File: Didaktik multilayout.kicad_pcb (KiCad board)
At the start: 2 copper layers, 209.6 x 76.2 mm, 125 parts, among them J1 Conn_01x04_MountingPin, J2 AVR-ISP-6, J3 Conn_01x03, SW1 SW_Push_45deg, SW10 SW_Push_45deg, SW11 SW_Push_45deg, SW12 SW_Push_45deg, SW13 SW_Push_45deg, SW14 SW_Push_45deg, SW15 SW_Push_45deg, SW16 SW_Push_45deg, SW17 SW_Push_45deg, SW18 SW_Push_45deg, SW19 SW_Push_45deg, SW2 SW_Push_45deg, SW20 SW_Push_45deg, SW21 SW_Push_45deg, SW22 SW_Push_45deg, SW23 SW_Push_45deg, SW24 SW_Push_45deg, SW25 SW_Push_45deg, SW26 SW_Push_45deg, SW27 SW_Push_45deg, SW28 SW_Push_45deg, SW29 SW_Push_45deg, SW3 SW_Push_45deg, SW30 SW_Push_45deg, SW31 SW_Push_45deg, SW31a1 SW_Push_45deg, SW32 SW_Push_45deg, SW32a1 SW_Push_45deg, SW33 SW_Push_45deg, SW33a1 SW_Push_45deg, SW34 SW_Push_45deg, SW34a1 SW_Push_45deg, SW34b1 SW_Push_45deg, SW35 SW_Push_45deg, SW35a1 SW_Push_45deg, SW35b1 SW_Push_45deg, SW35c1 SW_Push_45deg, SW36 SW_Push_45deg, SW36a1 SW_Push_45deg, SW36b1 SW_Push_45deg, SW36c1 SW_Push_45deg, SW37 SW_Push_45deg, SW37a1 SW_Push_45deg, SW37b1 SW_Push_45deg, SW38 SW_Push_45deg, SW38a1 SW_Push_45deg, SW39 SW_Push_45deg, SW39a1 SW_Push_45deg, SW4 SW_Push_45deg, SW40 SW_Push_45deg, SW40a1 SW_Push_45deg, SW41 RotaryEncoder_Switch, SW42 RotaryEncoder_Switch, SW5 SW_Push_45deg, SW6 SW_Push_45deg, SW7 SW_Push_45deg, SW8 SW_Push_45deg, SW9 SW_Push_45deg, U1 ATmega32U4-M, Y1 Crystal_GND24_Small

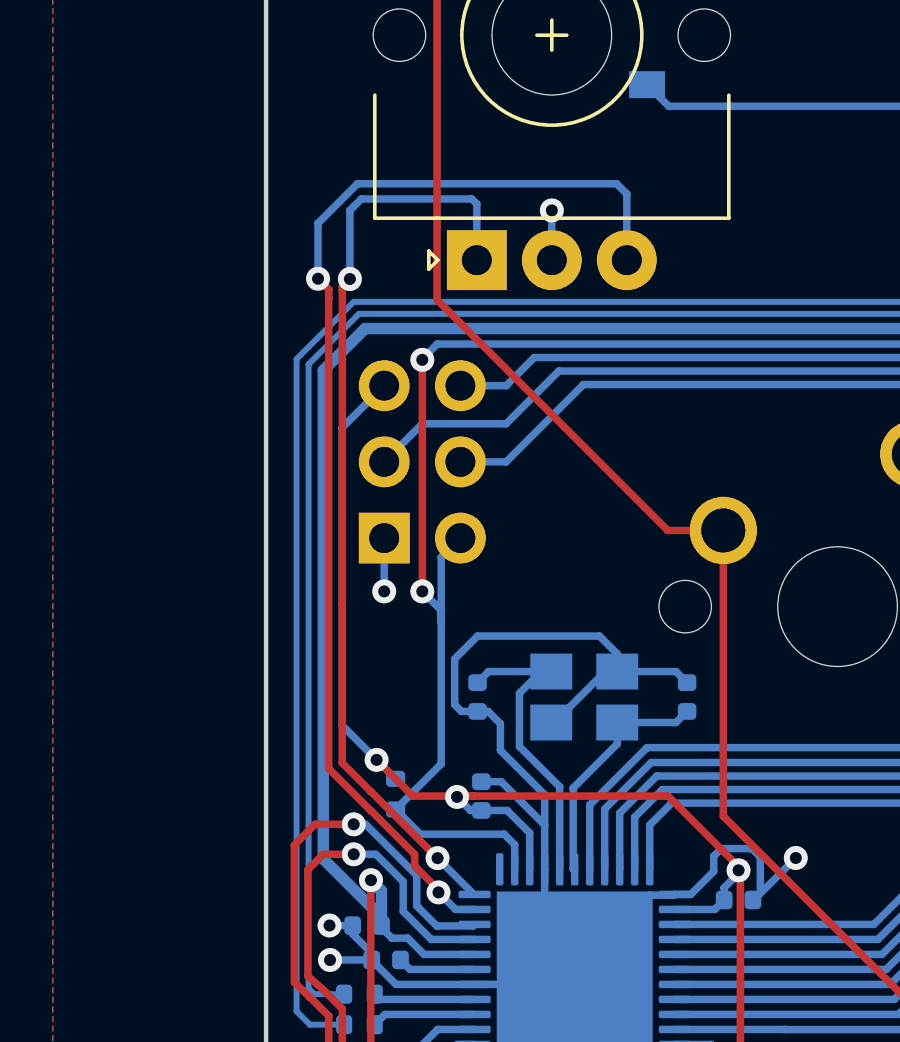
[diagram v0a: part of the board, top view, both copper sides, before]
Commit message: trying to export plate files
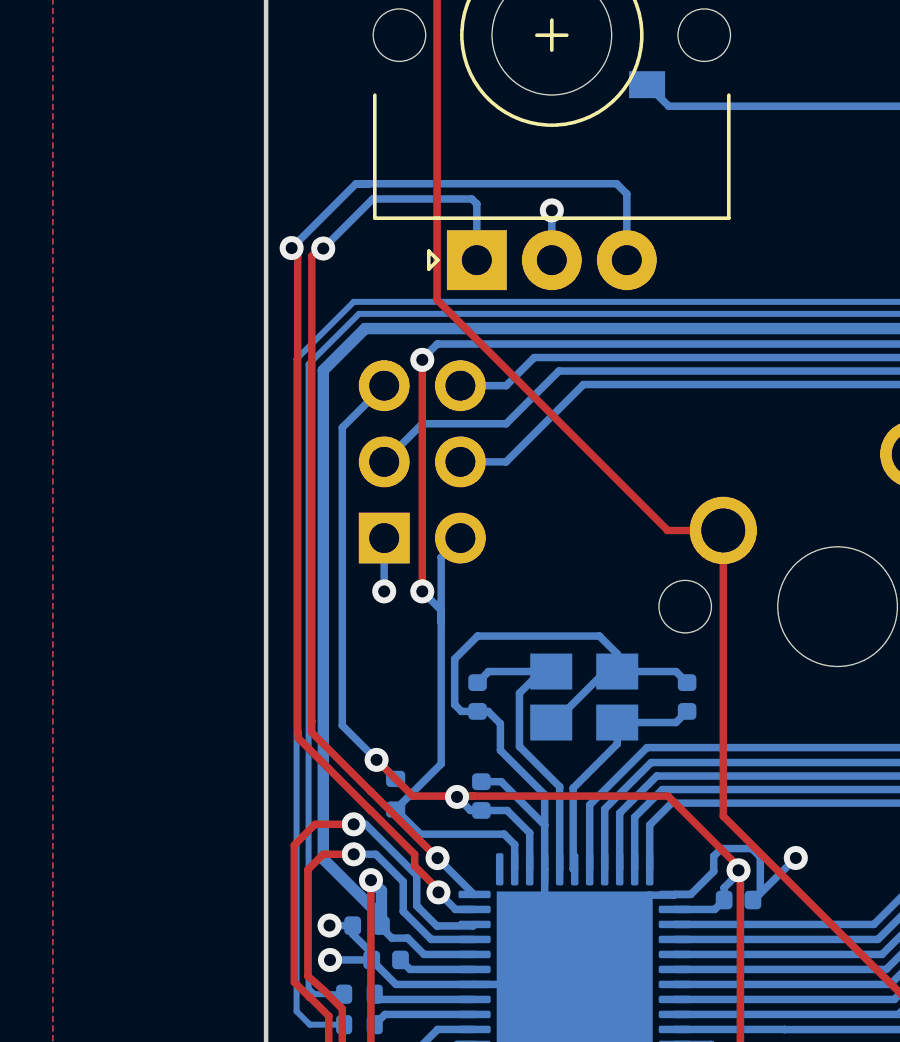
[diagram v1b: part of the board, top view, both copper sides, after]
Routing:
- net ROTARY_B: track 38.6 -> 39.8 mm
- net ROTARY_A: track 31.1 -> 31.8 mm
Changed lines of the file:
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@@
   (segment (start 47.018 70.104) (end 47.018 69.695) (width 0.25) (layer "B.Cu") (net 57))
   (segment (start 35.687 52.959) (end 34.29 54.356) (width 0.25) (layer "B.Cu") (net 57))
-  (segment (start 37.465 68.707) (end 35.245398 66.487398) (width 0.25) (layer "F.Cu") (net 58))
-  (segment (start 34.29 60.198) (end 34.29 49.784) (width 0.25) (layer "F.Cu") (net 58))
-  (segment (start 34.29 49.784) (end 34.29 49.657) (width 0.25) (layer "F.Cu") (net 58))
-  (segment (start 35.245398 66.487398) (end 35.239602 66.487398) (width 0.25) (layer "F.Cu") (net 58))
-  (segment (start 35.239602 66.487398) (end 34.287102 65.534898) (width 0.25) (layer "F.Cu") (net 58))
-  (segment (start 34.287102 60.200898) (end 34.29 60.198) (width 0.25) (layer "F.Cu") (net 58))
-  (segment (start 34.287102 65.534898) (end 34.287102 60.200898) (width 0.25) (layer "F.Cu") (net 58))
-  (segment (start 34.29 49.657) (end 34.544 49.403) (width 0.25) (layer "F.Cu") (net 58))
-  (via (at 34.544 49.403) (size 0.8) (drill 0.4) (layers "F.Cu" "B.Cu") (net 58))
+  (segment (start 33.528 48.387) (end 33.655 48.387) (width 0.25) (layer "F.Cu") (net 58))
+  (segment (start 33.274 64.135) (end 33.274 64.521796) (width 0.25) (layer "F.Cu") (net 58))
+  (segment (start 33.274 48.641) (end 33.528 48.387) (width 0.25) (layer "F.Cu") (net 58))
+  (segment (start 35.239602 66.487398) (end 35.245398 66.487398) (width 0.25) (layer "F.Cu") (net 58))
+  (segment (start 35.245398 66.487398) (end 37.465 68.707) (width 0.25) (layer "F.Cu") (net 58))
+  (segment (start 33.274 64.135) (end 33.274 48.641) (width 0.25) (layer "F.Cu") (net 58))
+  (segment (start 33.274 64.521796) (end 35.239602 66.487398) (width 0.25) (layer "F.Cu") (net 58))
+  (via (at 33.655 48.387) (size 0.8) (drill 0.4) (layers "F.Cu" "B.Cu") (net 58))
   (via (at 37.465 68.707) (size 0.8) (drill 0.4) (layers "F.Cu" "B.Cu") (net 58))
+  (segment (start 38.775 46.903) (end 38.775 48.775) (width 0.25) (layer "B.Cu") (net 58))
   (segment (start 38.67575 69.91775) (end 37.465 68.707) (width 0.25) (layer "B.Cu") (net 58))
-  (segment (start 34.544 49.403) (end 34.544 47.117) (width 0.25) (layer "B.Cu") (net 58))
-  (segment (start 34.544 47.117) (end 34.671 46.99) (width 0.25) (layer "B.Cu") (net 58))
   (segment (start 38.608 46.736) (end 38.775 46.903) (width 0.25) (layer "B.Cu") (net 58))
-  (segment (start 34.925 46.736) (end 38.608 46.736) (width 0.25) (layer "B.Cu") (net 58))
-  (segment (start 38.775 46.903) (end 38.775 48.775) (width 0.25) (layer "B.Cu") (net 58))
-  (segment (start 34.671 46.99) (end 34.925 46.736) (width 0.25) (layer "B.Cu") (net 58))
+  (segment (start 35.306 46.736) (end 38.608 46.736) (width 0.25) (layer "B.Cu") (net 58))
+  (segment (start 33.655 48.387) (end 35.306 46.736) (width 0.25) (layer "B.Cu") (net 58))
   (segment (start 38.6995 69.91775) (end 38.67575 69.91775) (width 0.25) (layer "B.Cu") (net 58))
   (segment (start 151.765 95.885) (end 147.0025 95.885) (width 0.25) (layer "F.Cu") (net 59))
@@
   (segment (start 48.729188 81.45) (end 43.853812 81.45) (width 0.25) (layer "B.Cu") (net 76))
   (segment (start 94.615 76.835) (end 90.054 72.274) (width 0.25) (layer "B.Cu") (net 76))
+  (segment (start 32.824 64.708192) (end 32.824 64.516) (width 0.25) (layer "F.Cu") (net 77))
   (segment (start 35.238904 67.123096) (end 33.837102 65.721294) (width 0.25) (layer "F.Cu") (net 77))
-  (segment (start 33.837102 50.040898) (end 33.84 50.038) (width 0.25) (layer "F.Cu") (net 77))
+  (segment (start 33.837102 65.721294) (end 32.824 64.708192) (width 0.25) (layer "F.Cu") (net 77))
+  (segment (start 32.803 48.661503) (end 32.528497 48.387) (width 0.25) (layer "F.Cu") (net 77))
+  (segment (start 32.803 64.495) (end 32.803 48.661503) (width 0.25) (layer "F.Cu") (net 77))
   (segment (start 36.702302 68.969607) (end 36.702302 68.580698) (width 0.25) (layer "F.Cu") (net 77))
   (segment (start 37.4965 69.763805) (end 36.702302 68.969607) (width 0.25) (layer "F.Cu") (net 77))
-  (segment (start 33.837102 65.721294) (end 33.837102 50.040898) (width 0.25) (layer "F.Cu") (net 77))
-  (segment (start 33.84 49.753136) (end 33.48093 49.394066) (width 0.25) (layer "F.Cu") (net 77))
-  (segment (start 33.84 50.038) (end 33.84 49.753136) (width 0.25) (layer "F.Cu") (net 77))
+  (segment (start 32.824 64.516) (end 32.803 64.495) (width 0.25) (layer "F.Cu") (net 77))
+  (segment (start 32.586245 48.387) (end 32.601318 48.371927) (width 0.25) (layer "F.Cu") (net 77))
+  (segment (start 32.528497 48.387) (end 32.586245 48.387) (width 0.25) (layer "F.Cu") (net 77))
   (segment (start 37.4965 69.85) (end 37.4965 69.763805) (width 0.25) (layer "F.Cu") (net 77))
   (segment (start 36.702302 68.580698) (end 35.248799 67.127195) (width 0.25) (layer "F.Cu") (net 77))
   (via (at 37.4965 69.85) (size 0.8) (drill 0.4) (layers "F.Cu" "B.Cu") (net 77))
-  (via (at 33.48093 49.394066) (size 0.8) (drill 0.4) (layers "F.Cu" "B.Cu") (net 77))
+  (via (at 32.601318 48.371927) (size 0.8) (drill 0.4) (layers "F.Cu" "B.Cu") (net 77))
   (arc (start 35.248799 67.127195) (mid 35.244259 67.124161) (end 35.238904 67.123096) (width 0.25) (layer "F.Cu") (net 77))
   (segment (start 43.775 46.569) (end 43.775 48.775) (width 0.25) (layer "B.Cu") (net 77))
-  (segment (start 33.48093 47.543674) (end 34.796604 46.228) (width 0.25) (layer "B.Cu") (net 77))
-  (segment (start 34.796604 46.228) (end 43.434 46.228) (width 0.25) (layer "B.Cu") (net 77))
   (segment (start 38.6995 70.41775) (end 38.06425 70.41775) (width 0.25) (layer "B.Cu") (net 77))
+  (segment (start 32.601318 48.371927) (end 34.745245 46.228) (width 0.25) (layer "B.Cu") (net 77))
+  (segment (start 34.796604 46.228) (end 34.925 46.228) (width 0.25) (layer "B.Cu") (net 77))
   (segment (start 38.06425 70.41775) (end 37.4965 69.85) (width 0.25) (layer "B.Cu") (net 77))
-  (segment (start 33.48093 49.394066) (end 33.48093 47.543674) (width 0.25) (layer "B.Cu") (net 77))
+  (segment (start 34.745245 46.228) (end 35.179 46.228) (width 0.25) (layer "B.Cu") (net 77))
   (segment (start 43.434 46.228) (end 43.775 46.569) (width 0.25) (layer "B.Cu") (net 77))
+  (segment (start 34.925 46.228) (end 35.179 46.228) (width 0.25) (layer "B.Cu") (net 77))
+  (segment (start 35.179 46.228) (end 43.434 46.228) (width 0.25) (layer "B.Cu") (net 77))
   (segment (start 34.29 78.613) (end 34.654503 78.977503) (width 0.25) (layer "F.Cu") (net 78))
   (segment (start 33.655 68.58) (end 33.1405 69.0945) (width 0.25) (layer "F.Cu") (net 78))

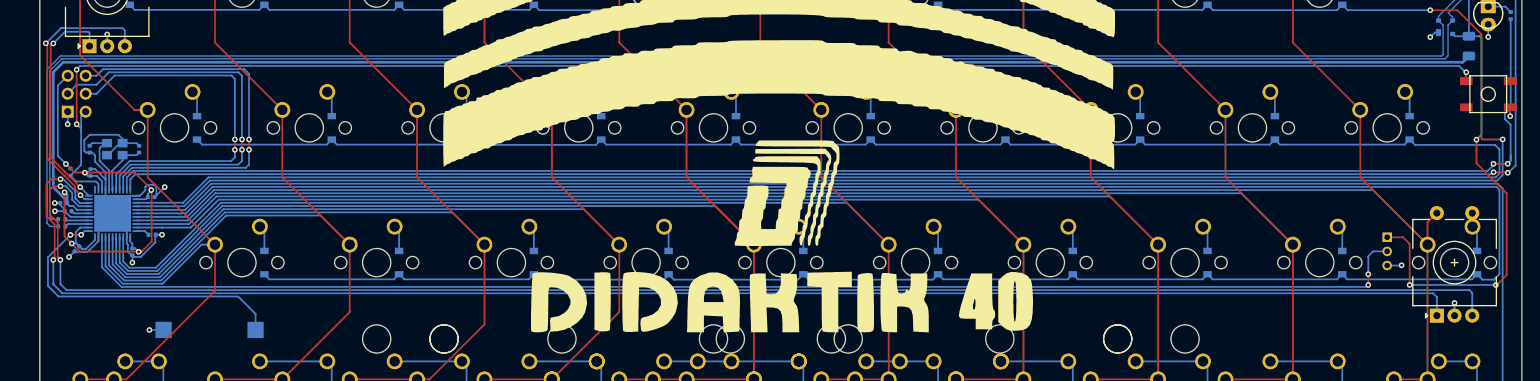
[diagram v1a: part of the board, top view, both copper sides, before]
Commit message: edited buzzer schematics & pcb placement
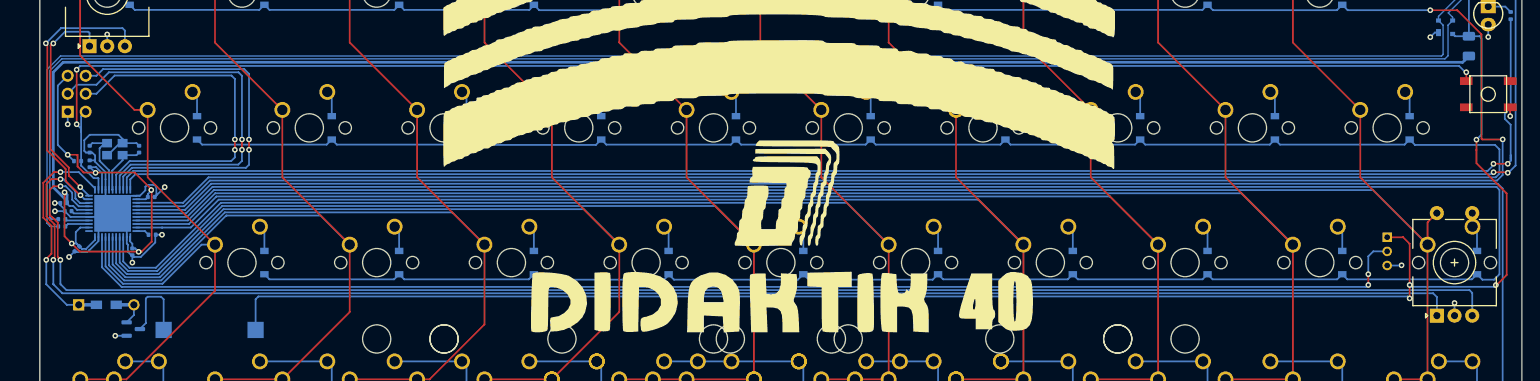
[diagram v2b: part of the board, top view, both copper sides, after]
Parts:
- added Q1: 2N2222, Package_TO_SOT_SMD:SOT-23, B.Cu at (45.0, 88.8)
- added R5: 1k, Keebio-Parts:Diode-Hybrid-Back, F.Cu at (41.1, 85.3)
- moved R3 1.85 mm to (37.1, 65.0), turned to 0 degrees
- moved C1 1.24 mm to (38.8, 65.4)
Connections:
- LS1 pad 1: Net-(U1-Pad1) -> VCC
- LS1 pad 2: GND -> Net-(LS1-Pad2)
- U1 pad 1: Net-(U1-Pad1) -> unconnected-(U1-Pad1)
- U1 pad 12: unconnected-(U1-Pad12) -> Net-(R5-Pad1)
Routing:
- net VCC: track 84.0 -> 253.6 mm, vias 3 -> 4
- net Net-(U1-Pad1): track 44.6 -> 0.00 mm, vias 2 -> 0
- net Net-(R5-Pad1): track 0.00 -> 30.0 mm, vias 0 -> 2
- net Net-(LS1-Pad2): track 0.00 -> 11.8 mm
- net Net-(Q1-Pad2): track 0.00 -> 2.90 mm
- net RESET: track 222.6 -> 220.0 mm
- net GND: track 91.4 -> 89.1 mm
- net +5V: track 301.0 -> 302.3 mm

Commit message: new production files
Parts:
- added R6: 1k, Resistor_SMD:R_0402_1005Metric, B.Cu at (55.8, 84.5)
- moved LS1 0.89 mm to (55.8, 89.8)
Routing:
- net VCC: track 253.6 -> 261.2 mm
- net Net-(Q1-Pad3): track 11.8 -> 19.1 mm
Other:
- board text added: "RESET"
- board text added: "resistor buzzer"
- board text removed: "JST"

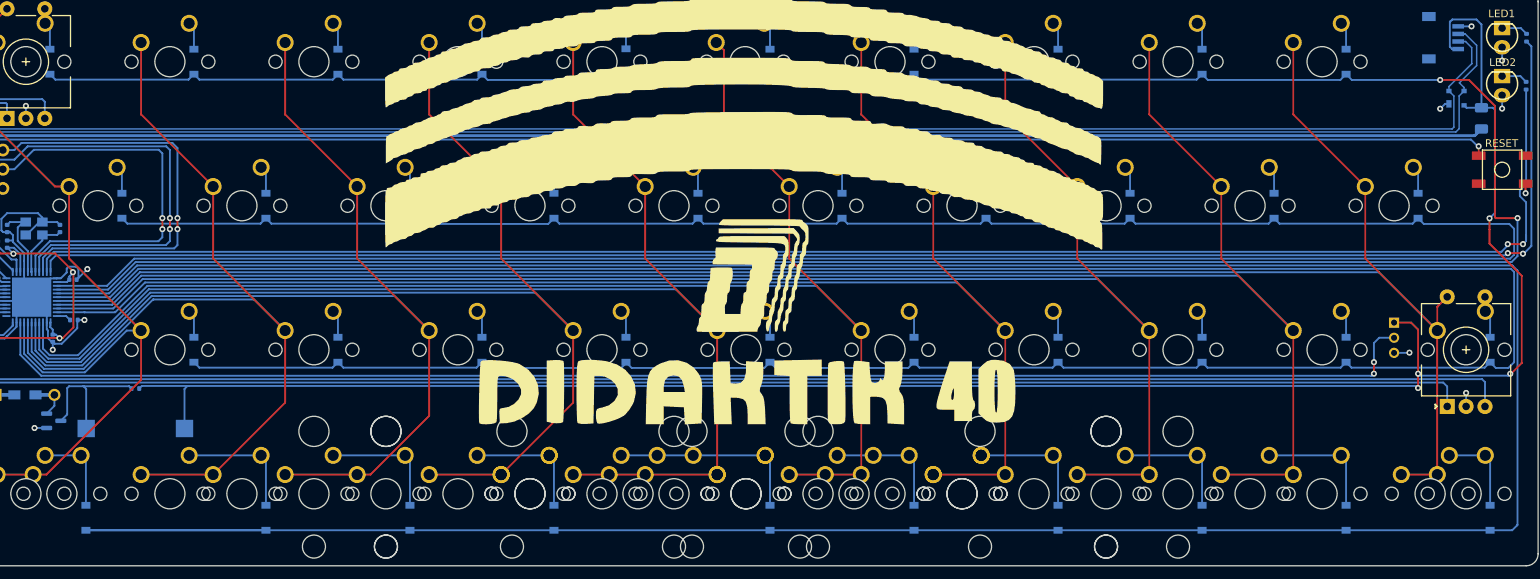
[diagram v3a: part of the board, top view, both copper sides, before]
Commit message: changed sod123 to sod123f
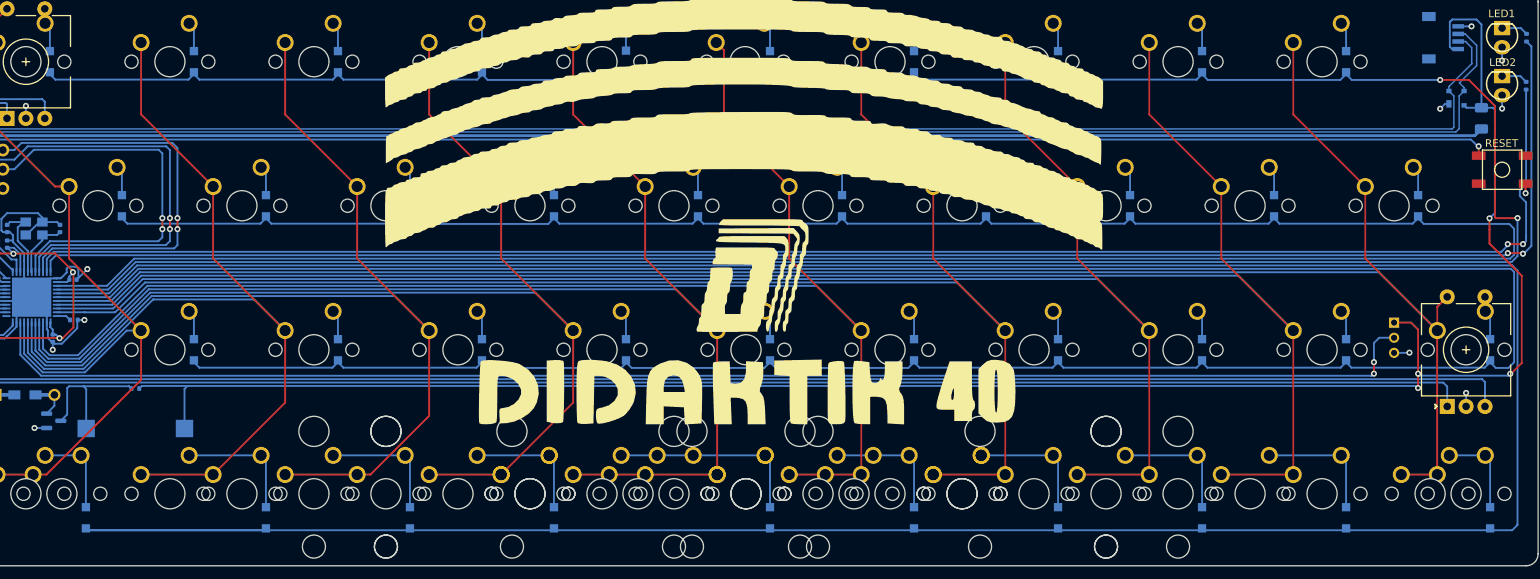
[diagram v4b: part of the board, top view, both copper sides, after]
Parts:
- D1, D10, D11, D12, D13, D14, D15, D16, D17, D18, D19, D2, D20, D21, D22, D23, D24, D26, D27, D28, D29, D3, D30, D31, D32, D33, D34, D35, D36, D37, D38, D39, D4, D40, D41, D5, D6, D7, D8, D9: footprint Diode_SMD:D_SOD-123 -> Diode_SMD:D_SOD-123F
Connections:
- net Net-(R5-Pad1) renamed SPEAKER

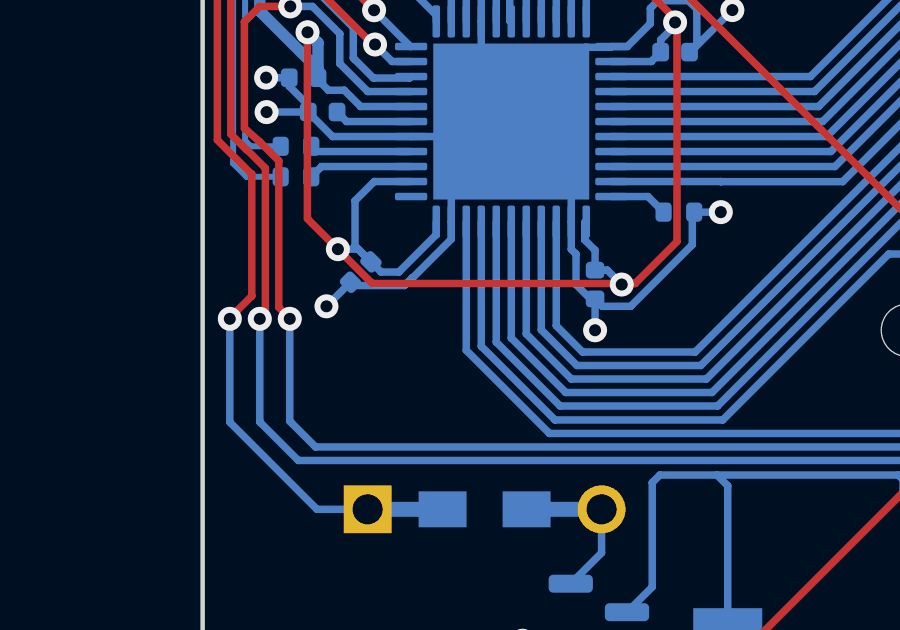
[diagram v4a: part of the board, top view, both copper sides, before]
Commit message: rgb pin changed from 42 to 1, new production files
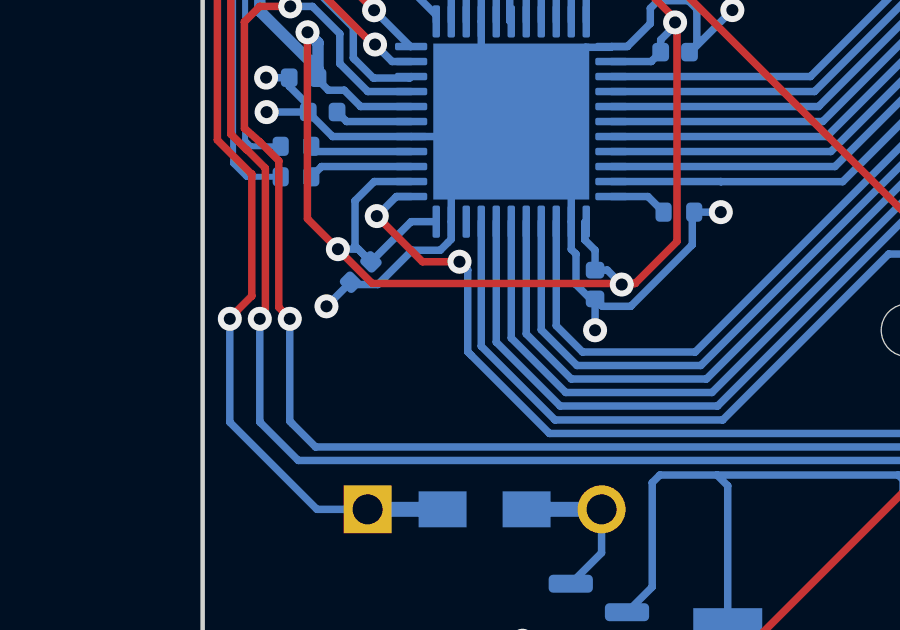
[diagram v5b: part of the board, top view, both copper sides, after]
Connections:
- U1 pad 1: unconnected-(U1-Pad1) -> RGB
- U1 pad 42: RGB -> unconnected-(U1-Pad42)
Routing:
- net RGB: track 191.6 -> 195.2 mm, vias 2 -> 4
- net +5V: track 302.3 -> 301.8 mm
